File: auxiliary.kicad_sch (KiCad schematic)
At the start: 30 parts

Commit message: More changes from review
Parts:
- removed C? (x4): C_1u_0603, antmicro-footprints:0603-cap, symbol antmicroCapacitors0603:C_1u_0603
- removed J?: WE_68715014522_ONE-SIDE, antmicro-footprints:WE_68715014522_ONE-SIDE, symbol antmicroFCCConnectors:WE_68715014522_ONE-SIDE
- removed J?: WE_68715014022, antmicro-footprints:WE_68715014022, symbol antmicroFCCConnectors:WE_68715014022
- added C? (x3): (no value), symbol antmicroCapacitors0402:C_100n_0402
- added J?: BM04B-SRSS-TB-LF-SN, antmicro-footprints:BM04B-SRSS-TB-LF-SN, symbol antmicroRectangularConnectorsHeadersMalePins:BM04B-SRSS-TB-LF-SN
- added R? (x12): (no value), symbol antmicroResistors0402:R_0R_0402
- added R? (x2): (no value), symbol antmicroResistors0402:R_2k2_0402
- added R? (x10): (no value), symbol antmicroResistors0402:R_2k_0402
- added R? (x2): ~, symbol antmicroResistors0402:R_2k2_0402
- added R?: (no value), symbol antmicroResistors0402:R_10k_0402
- added SP? (x3): 9774110360, antmicro-footprints:Mounting_Wuerth_WA-SMSI-M3_H11mm_9774110360, symbol antmicroMechanicalParts:9774110360
- added TP? (x10): (no value), symbol antmicroTestPoints:TP
- added U?: (no value), symbol antmicroLogicSignalSwitchesMultiplexersDecoders:PCA9547BS,118
- added U?: (no value), symbol antmicroLogicTranslatorsLevelShifters:NTS0102DP
- C? (x2): value C_100n_0402 -> (none); footprint antmicro-footprints:0402-cap -> (none)
- C?: value C_220n_0402 -> (none); footprint antmicro-footprints:0402-cap -> (none)
- C? (x2): value C_220u_KEMET_D -> (none); footprint antmicro-footprints:KEMET_D -> (none)
- D?: value B340A-13-F -> (none); footprint antmicro-footprints:DO-214AC -> (none)
- IC?: value MAX1708EEE+ -> (none); footprint antmicro-footprints:QSOP-16_3.9x4.9mm_P0.635mm -> (none)
- J?: value SM06B-SRSS-TB(LF)(SN) -> (none); footprint antmicro-footprints:JST_SM06B-SRSS-TB(LF)(SN) -> (none)
- J?: value SM09B-SRSS-TB(LF)(SN) -> (none); footprint antmicro-footprints:JST_SM09B-SRSS-TB(LF)(SN) -> (none)
- J?: value 61300611121 -> (none); footprint antmicro-footprints:61300611121 -> (none)
- L?: value IHLP2525CZER2R2M01 -> (none); footprint antmicro-footprints:IHLP2525CZER -> (none)
- Q?: value BSS138AKA -> (none); footprint antmicro-footprints:SOT-23-3 -> (none)
- R?: value R_2R_0402 -> (none); footprint antmicro-footprints:0402-res -> (none)
- R? (x4): value R_2k_0402 -> (none); footprint antmicro-footprints:0402-res -> (none)
- R? (x5): value R_0R_0402 -> (none); footprint antmicro-footprints:0402-res -> (none)
- TP? (x2): value TP -> (none); footprint antmicro-footprints:TP-R-1.5 -> (none)
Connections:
- net +3V3: now also C?.1, C?.1, J?.2 (Pin_2), R?.1, R?.1, R?.2, R?.2, R?.2, R?.2, R?.2, R?.2, R?.2, R?.2, R?.2, R?.2, R?.2, R?.2, R?.2, R?.2, U?.21 (VCC), U?.7 (VCC_B)
- net CAM0_SCL: now also R?.1, R?.2, TP?.1
- net CAM0_SDA: now also R?.1, R?.2, TP?.1
- net CAM1_SCL: now also R?.1, R?.2, TP?.1
- net CAM1_SDA: now also R?.1, R?.2, TP?.1
- net CAM2_SCL: now also R?.1, R?.2, TP?.1
- net CAM2_SDA: now also R?.1, R?.2, TP?.1
- net CAM3_SCL: now also R?.1, R?.2, TP?.1
- net CAM3_SDA: now also R?.1, R?.2, TP?.1
- net GND: now also C?.2, C?.2, C?.2, J?.1 (Pin_1), R?.1, U?.18 (A2), U?.2 (GND), U?.23 (A1), U?.25 (GND), U?.9 (GND)
- new net: R?.1, U?.2 (SC0)
- new net: R?.1, U?.1 (SD0)
- new net: R?.1, U?.5 (SD2)
- new net: R?.1, R?.2, U?.22 (A0)
- new net: R?.1, U?.8 (SC3)
- new net: R?.2, U?.19 (SCL)
- new net: R?.1, U?.6 (SC2)
- new net: R?.2, U?.20 (SDA)
- new net: R?.1, U?.24 (~{RESET})
- new net: R?.1, U?.3 (SD1)
- new net: R?.1, U?.4 (SC1)
- new net: R?.1, U?.7 (SD3)
- new net +1V8: C?.1, U?.3 (VCC_A), U?.6 (OE)
- new net AUX_I2C_SCL: J?.4 (Pin_4), R?.2, U?.15 (SC6)
- new net AUX_I2C_SDA: J?.3 (Pin_3), R?.1, U?.14 (SD6)
- new net I2C_GP3_CLK: TP?.1, U?.4 (A2)
- new net I2C_GP3_DAT: TP?.1, U?.5 (A1)
- new net MISC_I2C_SCL: R?.2, U?.17 (SC7)
- new net MISC_I2C_SDA: R?.1, U?.16 (SD7)
- new net SCL_3V3: R?.1, R?.1, U?.1 (B2)
- new net SDA_3V3: R?.1, R?.1, U?.8 (B1)
- no-connect marks 36 -> 12
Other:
- note added: "0b1110000R"
- note added: "0x70h"
- note added: "GPIO Connector"
- note added: "I2C Level Shifting"
- note added: "I2C Multiplexer"
- note added: "I2C address:"
- note added: "Mounting standoffs"
- note added: "To camera I2C interfaces"
- note removed: "Bottom CSI"
- note removed: "CAM 0"
- note removed: "CAM 1"
- note removed: "CAM 2"
- note removed: "CAM 3"
- note removed: "CAM3"
- note removed: "CSI 0"
- note removed: "CSI 1"
- note removed: "CSI 2"
- note removed: "CSI 3"
- note removed: "CSI 4"
- note removed: "CSI 5"
- note removed: "CSI 6"
- note removed: "CSI 7"
- note removed: "Camera module interfaces"
- note removed: "Control interface"
- note removed: "RealSense sync connector"
- note removed: "Side CSI"

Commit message: Add TVS to wire connectors
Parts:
- added D? (x3): PUSB3F96X_PASS, antmicro-footprints:PUSB3F96X, symbol antmicroTVSDiodes:PUSB3F96X_PASS
- C? (x5): value (none) -> C_100n_0402; footprint (none) -> antmicro-footprints:0402-cap
- C?: value (none) -> C_220n_0402; footprint (none) -> antmicro-footprints:0402-cap
- C? (x2): value (none) -> C_220u_KEMET_D; footprint (none) -> antmicro-footprints:KEMET_D
- D?: value (none) -> B340A-13-F; footprint (none) -> antmicro-footprints:DO-214AC
- IC?: value (none) -> MAX1708EEE+; footprint (none) -> antmicro-footprints:QSOP-16_3.9x4.9mm_P0.635mm
- J?: value (none) -> SM06B-SRSS-TB(LF)(SN); footprint (none) -> antmicro-footprints:JST_SM06B-SRSS-TB(LF)(SN)
- J?: value (none) -> SM09B-SRSS-TB(LF)(SN); footprint (none) -> antmicro-footprints:JST_SM09B-SRSS-TB(LF)(SN)
- J?: value (none) -> 61300611121; footprint (none) -> antmicro-footprints:61300611121
- L?: value (none) -> IHLP2525CZER2R2M01; footprint (none) -> antmicro-footprints:IHLP2525CZER
- Q?: value (none) -> BSS138AKA; footprint (none) -> antmicro-footprints:SOT-23-3
- R?: value (none) -> R_2R_0402; footprint (none) -> antmicro-footprints:0402-res
- R? (x14): value (none) -> R_2k_0402; footprint (none) -> antmicro-footprints:0402-res
- R? (x17): value (none) -> R_0R_0402; footprint (none) -> antmicro-footprints:0402-res
- R? (x2): value (none) -> R_2k2_0402; footprint (none) -> antmicro-footprints:0402-res
- R?: value (none) -> R_10k_0402; footprint (none) -> antmicro-footprints:0402-res
- TP? (x12): value (none) -> TP; footprint (none) -> antmicro-footprints:TP-R-1.5
- U?: value (none) -> PCA9547BS,118; footprint (none) -> antmicro-footprints:HVQFN24
- U?: value (none) -> NTS0102DP; footprint (none) -> antmicro-footprints:TSSOP-8_W3mm
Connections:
- net AUX_I2C_SCL: now also D?.4 (CH3), D?.7 (CH3)
- net AUX_I2C_SDA: now also D?.5 (CH4), D?.6 (CH4)
- net CAM3_SCL: now also D?.1 (CH1), D?.10 (CH1)
- net CAM3_SDA: now also D?.2 (CH2), D?.9 (CH2)
- net DEPTH_CAM_SYNC: now also D?.2 (CH2), D?.9 (CH2)
- net DEPTH_CAM_SYNC_3V3: now also D?.1 (CH1), D?.10 (CH1)
- net GND: now also D?.3 (GND), D?.3 (GND), D?.3 (GND), D?.8 (GND), D?.8 (GND), D?.8 (GND)
- net VSYNC_CAM0_3V3: now also D?.1 (CH1), D?.10 (CH1)
- net VSYNC_CAM1_3V3: now also D?.2 (CH2), D?.9 (CH2)
- net VSYNC_CAM2_3V3: now also D?.4 (CH3), D?.7 (CH3)
- net VSYNC_CAM3_3V3: now also D?.5 (CH4), D?.6 (CH4)
- new net: D?.4 (CH3), D?.7 (CH3)
- new net: D?.5 (CH4), D?.6 (CH4)
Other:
- note added: "QWIIC Connector"
- note added: "Sync Connector"
- title: (none) -> Antmicro Jetson AGX CSI Adapter
- moved on the sheet: C?, D?, IC?, J?, L?, Q?, R?, SP?, TP?, U?

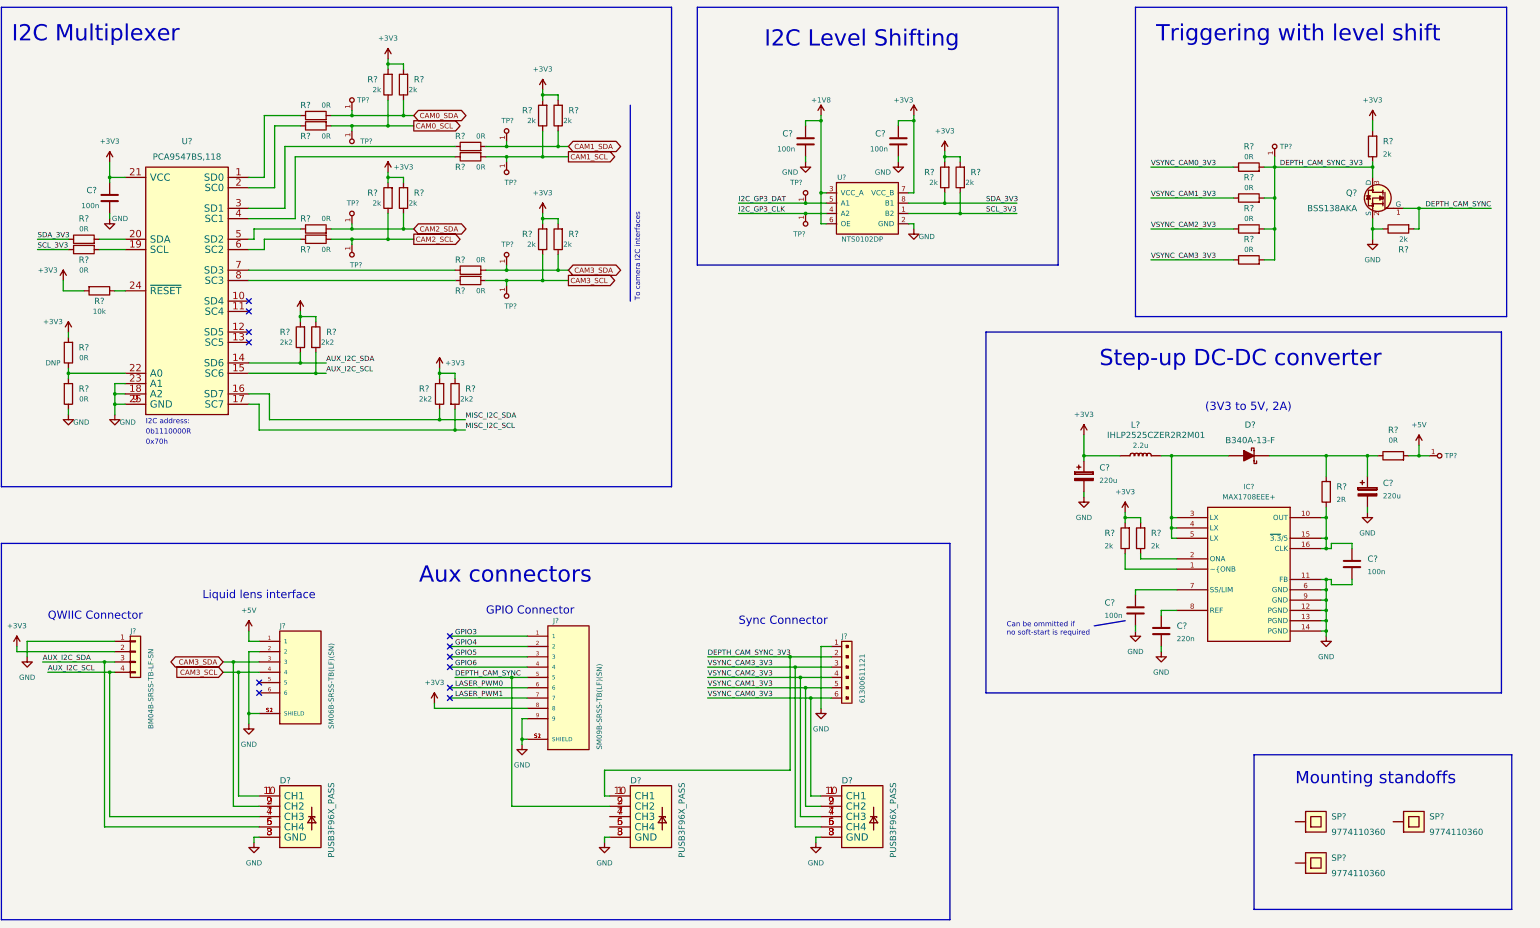
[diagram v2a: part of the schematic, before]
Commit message: Routed CSI interface
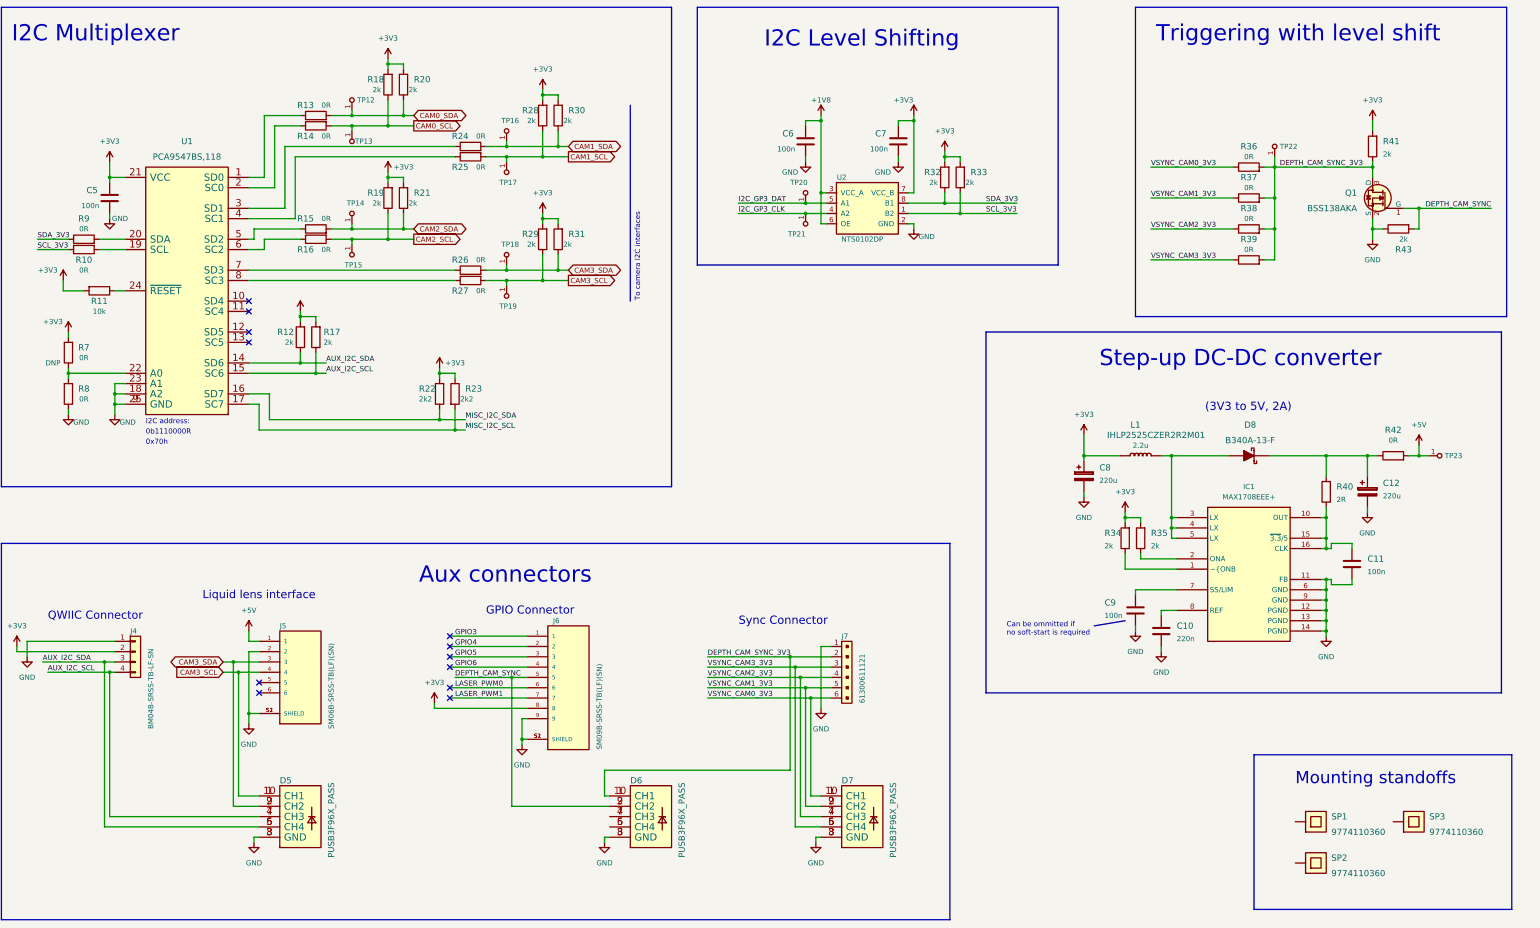
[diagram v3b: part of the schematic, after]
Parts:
- removed R? (x2): ~, symbol antmicroResistors0402:R_2k2_0402
- added R12, R17: R_2k_0402, antmicro-footprints:0402-res, symbol antmicroResistors0402:R_2k_0402
- gave numbers to parts that had none: 71
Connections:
- net +3V3: now also R12.2, R17.2
- net AUX_I2C_SCL: now also R17.1
- net AUX_I2C_SDA: now also R12.1

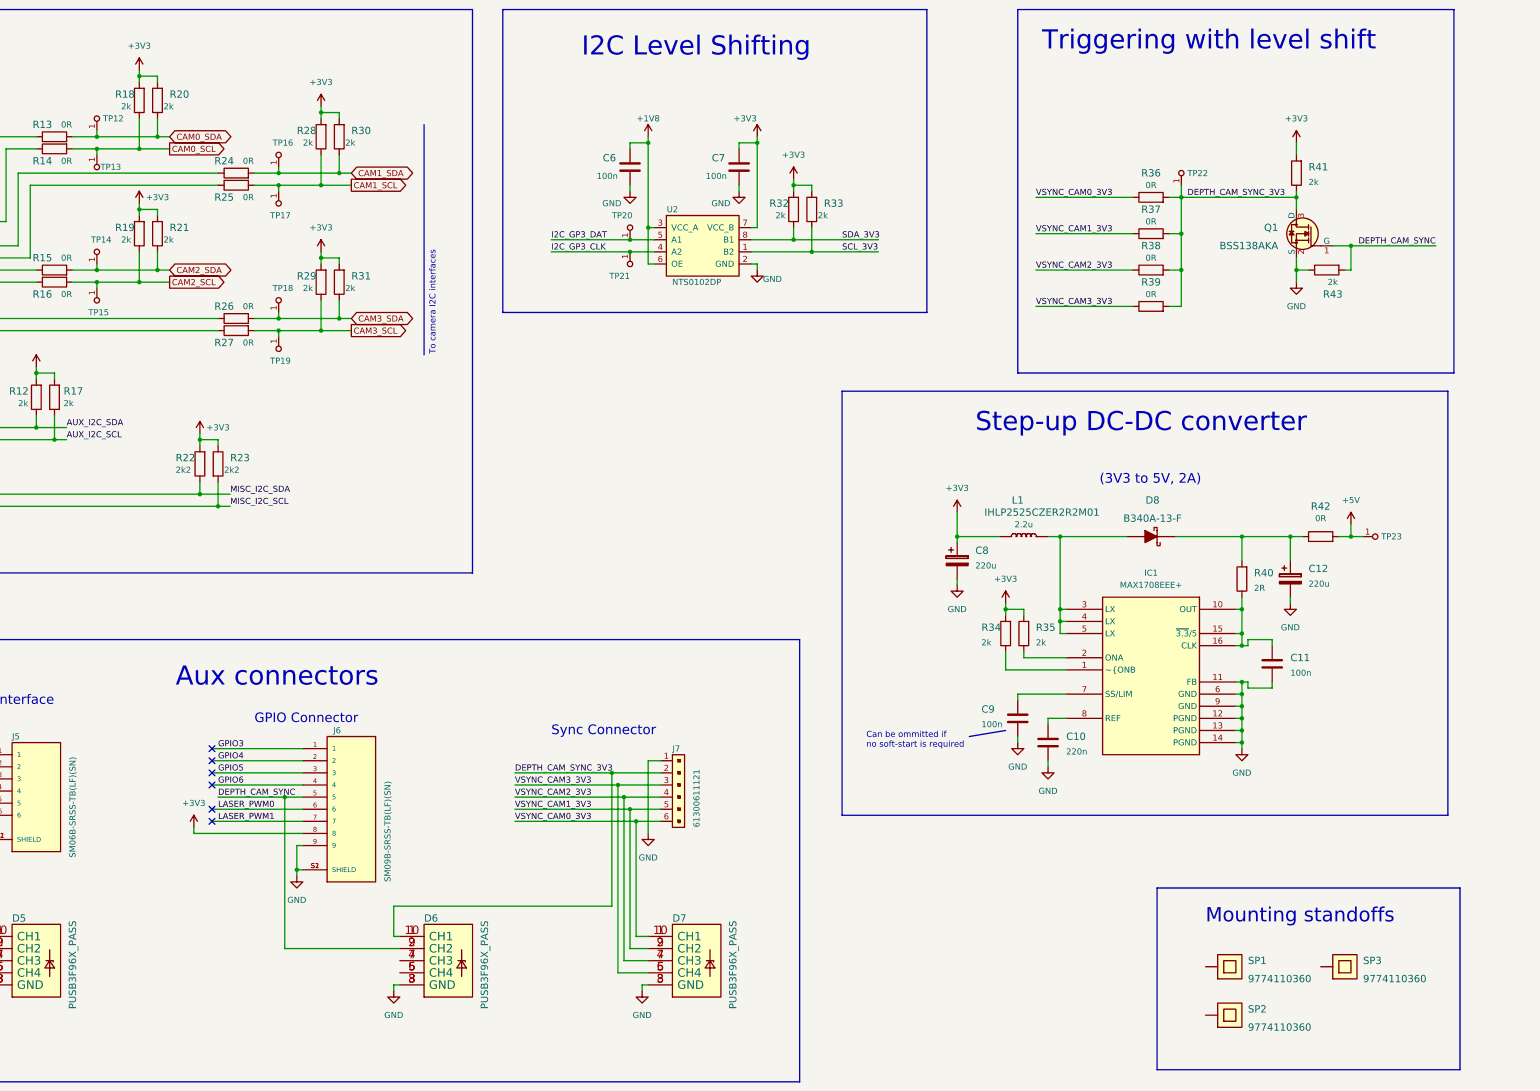
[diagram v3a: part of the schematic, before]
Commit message: Routed I2C signals, completed a layout of the voltage converter and I2C IC.
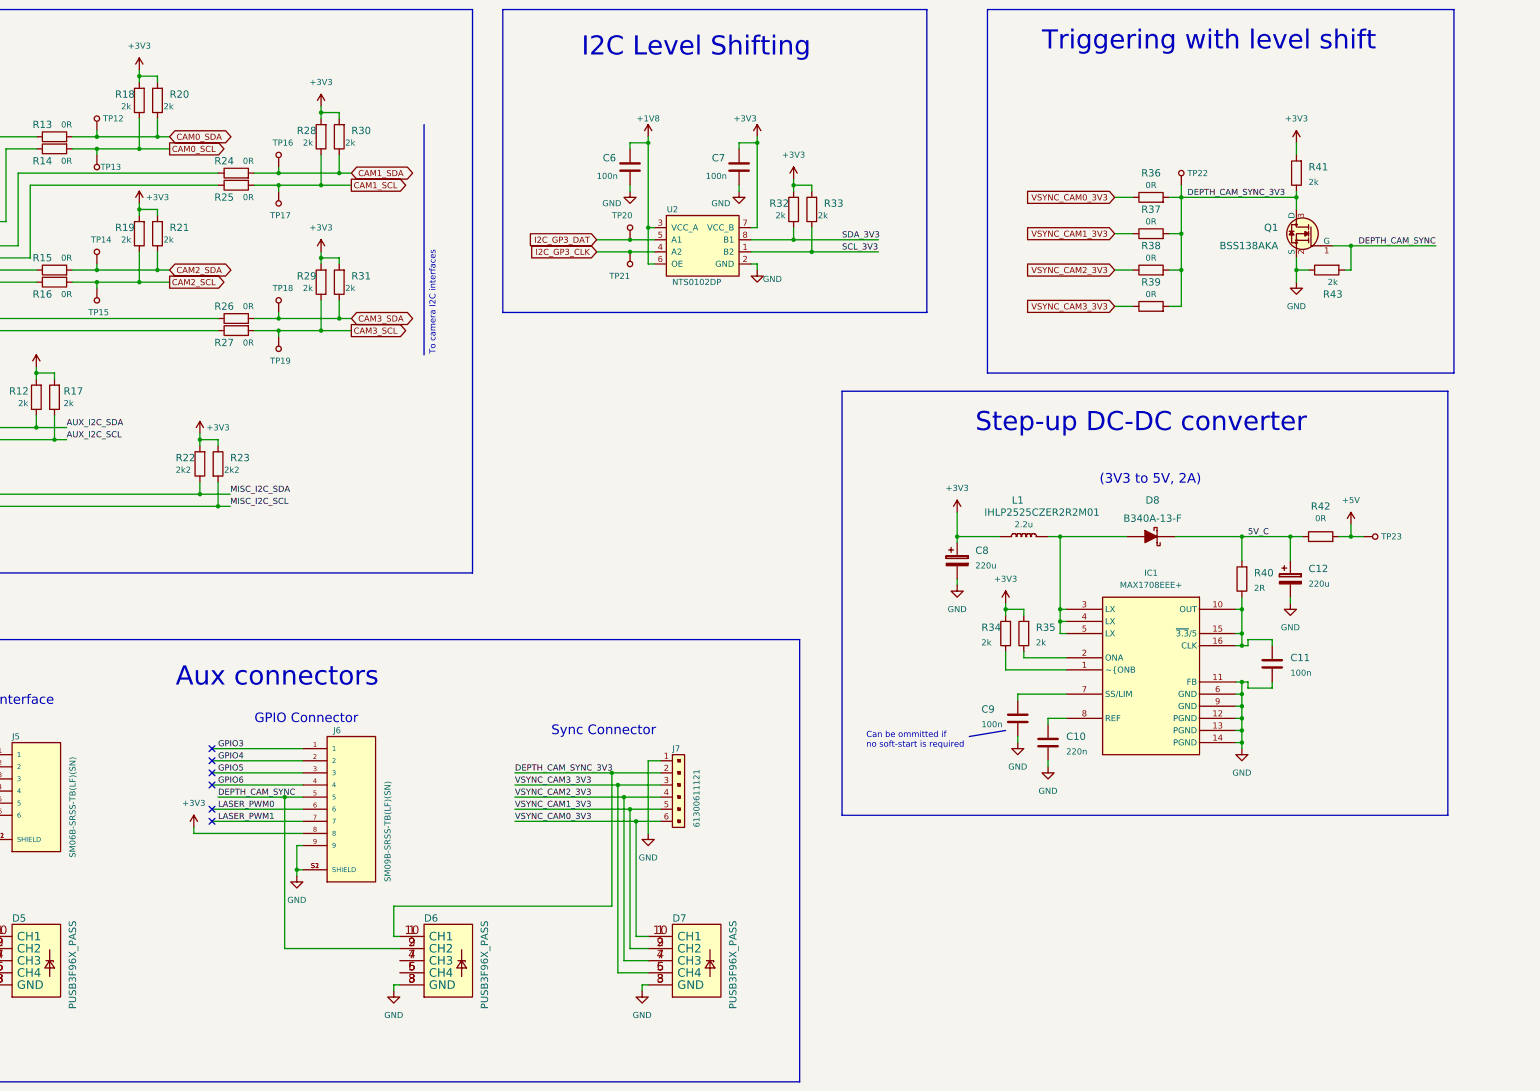
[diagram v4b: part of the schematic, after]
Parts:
- removed SP1, SP2, SP3: 9774110360, antmicro-footprints:Mounting_Wuerth_WA-SMSI-M3_H11mm_9774110360, symbol antmicroMechanicalParts:9774110360
- TP12, TP13, TP14, TP15, TP16, TP17, TP18, TP19, TP20, TP21, TP22, TP23: value TP -> TP_SMD_0_75MM; footprint antmicro-footprints:TP-R-1.5 -> antmicro-footprints:Testpoint_smd_0_75mm; symbol antmicroTestPoints:TP -> antmicroTestPoints:TP_SMD_0_75MM
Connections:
- net 5V_C: now reaches C12.1, D8.K, R40.2, R42.1
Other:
- note removed: "Mounting standoffs"
